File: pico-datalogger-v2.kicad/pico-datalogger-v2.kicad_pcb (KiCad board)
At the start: 2 copper layers, 46 x 60 mm, 35 parts, among them J1 JST-PH2 Bat, J10 Conn_PCB_2, J11 Conn_I2C1, J12 Conn_UART_5V, J13 Conn_I2C1, J14 Conn_I2C0, J2 Conn_Pico_Left, J3 Conn_Pico_Right, J4 Alt-Bat, J5 Conn_LoRa, J6 Conn_Display, J7 Conn_PCB_1, J8 Conn_ADC, J9 Conn_I2C0, Q1 AO3401A, SW1 SW_ON, SW2 SW_RUN, U1 74LVC2G74, U2 PCF8523T, U4 XTSD, Y1 Crystal

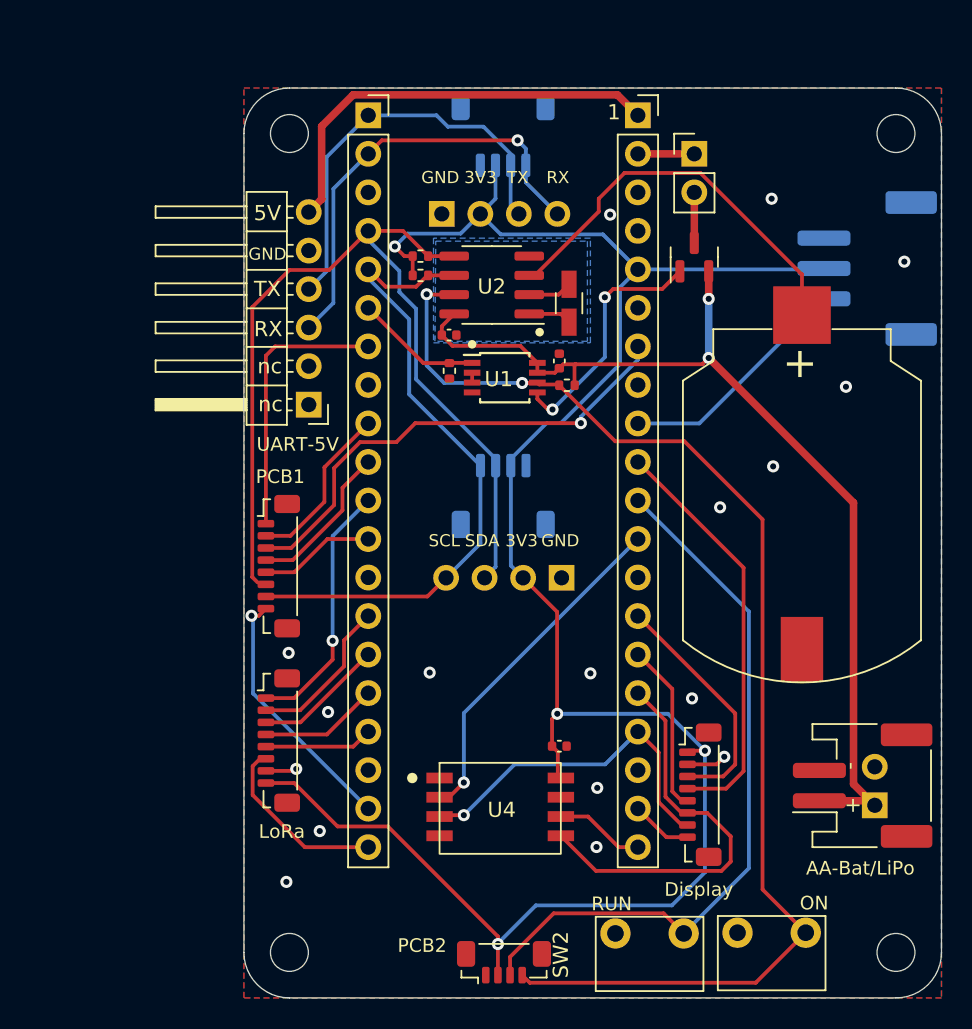
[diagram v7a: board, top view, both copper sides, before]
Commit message: Rev 0.94: use mosfet instead of jumper for VSYS
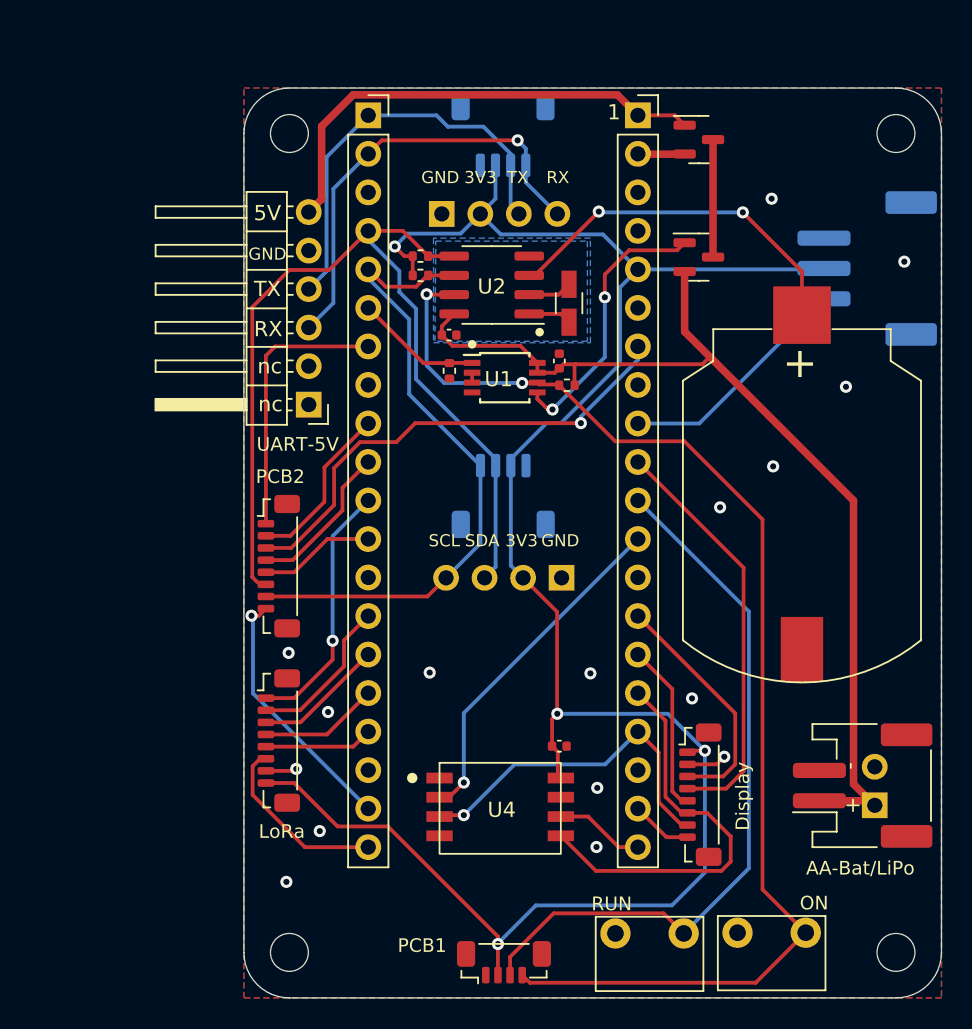
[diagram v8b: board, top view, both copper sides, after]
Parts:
- removed JP1: Jumper_VSYS, Connector_PinHeader_2.54mm:PinHeader_1x02_P2.54mm_Vertical
- added Q2: AO3401A, Package_TO_SOT_SMD:SOT-23, F.Cu at (130.0, 103.4)
- moved Q1 0.30 mm to (130.0, 111.2), turned to 0 degrees
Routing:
- net Net-(Q1-Pad3): track 3.28 -> 7.75 mm
- net /VBUS: track 28.3 -> 31.6 mm
- net Net-(BT1-Pad1): track 26.7 -> 24.2 mm, vias 0 -> 2
- net /PC_GATE: track 16.2 -> 18.2 mm
- net /VSYS: track 3.72 -> 2.78 mm
- net +BATT: track 66.1 -> 66.7 mm, vias 2 -> 0
- net GND: vias 17 -> 16
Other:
- board text added: "https://github.com/bablokb/pcb-pico-datalogger https://opendeved.net/ilce Rev 0.94"
- board text removed: "https://github.com/bablokb/pcb-pico-datalogger https://opendeved.net/ilce Rev 0.93"
